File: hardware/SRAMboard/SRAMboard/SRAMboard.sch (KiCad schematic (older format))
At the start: 0 parts

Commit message: SRAMboard I
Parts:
- added C1, C2: C, Capacitor_SMD:C_0805_2012Metric, symbol Device:C
- added J1, J2: Conn_02x13_Odd_Even, Connector_PinSocket_2.54mm:PinSocket_2x13_P2.54mm_Vertical, symbol Connector_Generic:Conn_02x13_Odd_Even
- added U1: IS66WV51216EBLL-70BLI, kifootp:BGA-48_6.0x8.0mm_Layout6x8_P0.75mm, symbol kilib:IS66WV51216EBLL-70BLI
- added U2: IS66WV51216EBLL-70TLI, Package_SO:TSOP-II-44_10.16x18.41mm_P0.8mm, symbol kilib:IS66WV51216EBLL-70TLI
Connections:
- new net +3V3: C1.1, J1.20 (Pin_20), U1.D6 (VDD), U2.33 (VDD)
- new net 3V3: C2.1, J1.18 (Pin_18), U1.E1 (VDD), U2.11 (VDD)
- new net A0: J1.1 (Pin_1), U1.A3 (A0), U2.5 (A0)
- new net A1: J1.3 (Pin_3), U1.A4 (A1), U2.4 (A1)
- new net A10: J1.21 (Pin_21), U1.H4 (A10), U2.25 (A10)
- new net A11: J1.23 (Pin_23), U1.H5 (A11), U2.24 (A11)
- new net A12: J1.2 (Pin_2), U1.G3 (A12), U2.22 (A12)
- new net A13: J1.4 (Pin_4), U1.G4 (A13), U2.21 (A13)
- new net A14: J1.6 (Pin_6), U1.F3 (A14), U2.20 (A14)
- new net A15: J1.8 (Pin_8), U1.F4 (A15), U2.19 (A15)
- new net A16: J1.10 (Pin_10), U1.E4 (A16), U2.18 (A16)
- new net A17: J1.12 (Pin_12), U1.D3 (A17), U2.23 (A17)
- new net A18: J1.14 (Pin_14), U1.H1 (A18), U2.28 (A18)
- new net A2: J1.5 (Pin_5), U1.A5 (A2), U2.3 (A2)
- new net A3: J1.7 (Pin_7), U1.B3 (A3), U2.2 (A3)
- new net A4: J1.9 (Pin_9), U1.B4 (A4), U2.1 (A4)
- new net A5: J1.11 (Pin_11), U1.C3 (A5), U2.44 (A5)
- new net A6: J1.13 (Pin_13), U1.C4 (A6), U2.43 (A6)
- new net A7: J1.15 (Pin_15), U1.D4 (A7), U2.42 (A7)
- new net A8: J1.17 (Pin_17), U1.H2 (A8), U2.27 (A8)
- new net A9: J1.19 (Pin_19), U1.H3 (A9), U2.26 (A9)
- new net CS0#: J2.1 (Pin_1), U2.6 (CS1#)
- new net CS1#: J2.3 (Pin_3), U1.B5 (CS1#)
- new net CS2: J2.5 (Pin_5), U1.A6 (CS2)
- new net GND: C1.2, C2.2, J1.16 (Pin_16), J1.22 (Pin_22), U1.D1 (GND), U1.E6 (GND), U2.12 (GND), U2.34 (GND)
- new net IO0: J2.15 (Pin_15), U1.B6 (I/O0), U2.7 (I/O0)
- new net IO1: J2.17 (Pin_17), U1.C5 (I/O1), U2.8 (I/O1)
- new net IO10: J2.10 (Pin_10), U1.C2 (I/O10), U2.31 (I/O10)
- new net IO11: J2.12 (Pin_12), U1.D2 (I/O11), U2.32 (I/O11)
- new net IO12: J2.14 (Pin_14), U1.E2 (I/O12), U2.35 (I/O12)
- new net IO13: J2.16 (Pin_16), U1.F2 (I/O13), U2.36 (I/O13)
- new net IO14: J2.18 (Pin_18), U1.F1 (I/O14), U2.37 (I/O14)
- new net IO15: J2.20 (Pin_20), U1.G1 (I/O15), U2.38 (I/O15)
- new net IO2: J2.19 (Pin_19), U1.C6 (I/O2), U2.9 (I/O2)
- new net IO3: J2.21 (Pin_21), U1.D5 (I/O3), U2.10 (I/O3)
- new net IO4: J2.23 (Pin_23), U1.E5 (I/O4), U2.13 (I/O4)
- new net IO5: J2.25 (Pin_25), U1.F5 (I/O5), U2.14 (I/O5)
- new net IO6: J2.2 (Pin_2), U1.F6 (I/O6), U2.15 (I/O6)
- new net IO7: J2.4 (Pin_4), U1.G6 (I/O7), U2.16 (I/O7)
- new net IO8: J2.6 (Pin_6), U1.B1 (I/O8), U2.29 (I/O8)
- new net IO9: J2.8 (Pin_8), U1.C1 (I/O9), U2.30 (I/O9)
- new net LB#: J2.13 (Pin_13), U1.A1 (LB#), U2.39 (LB#)
- new net NC0: J2.22 (Pin_22), U1.G2 (NC)
- new net NC1: J2.24 (Pin_24), U1.E3 (NC)
- new net NC2: J2.26 (Pin_26), U1.H6 (NC)
- new net OE#: J2.7 (Pin_7), U1.A2 (OE#), U2.41 (OE#)
- new net UB#: J2.11 (Pin_11), U1.B2 (UB#), U2.40 (UB#)
- new net WE#: J2.9 (Pin_9), U1.G5 (WE#), U2.17 (WE#)
- no-connect marks 0 -> 3

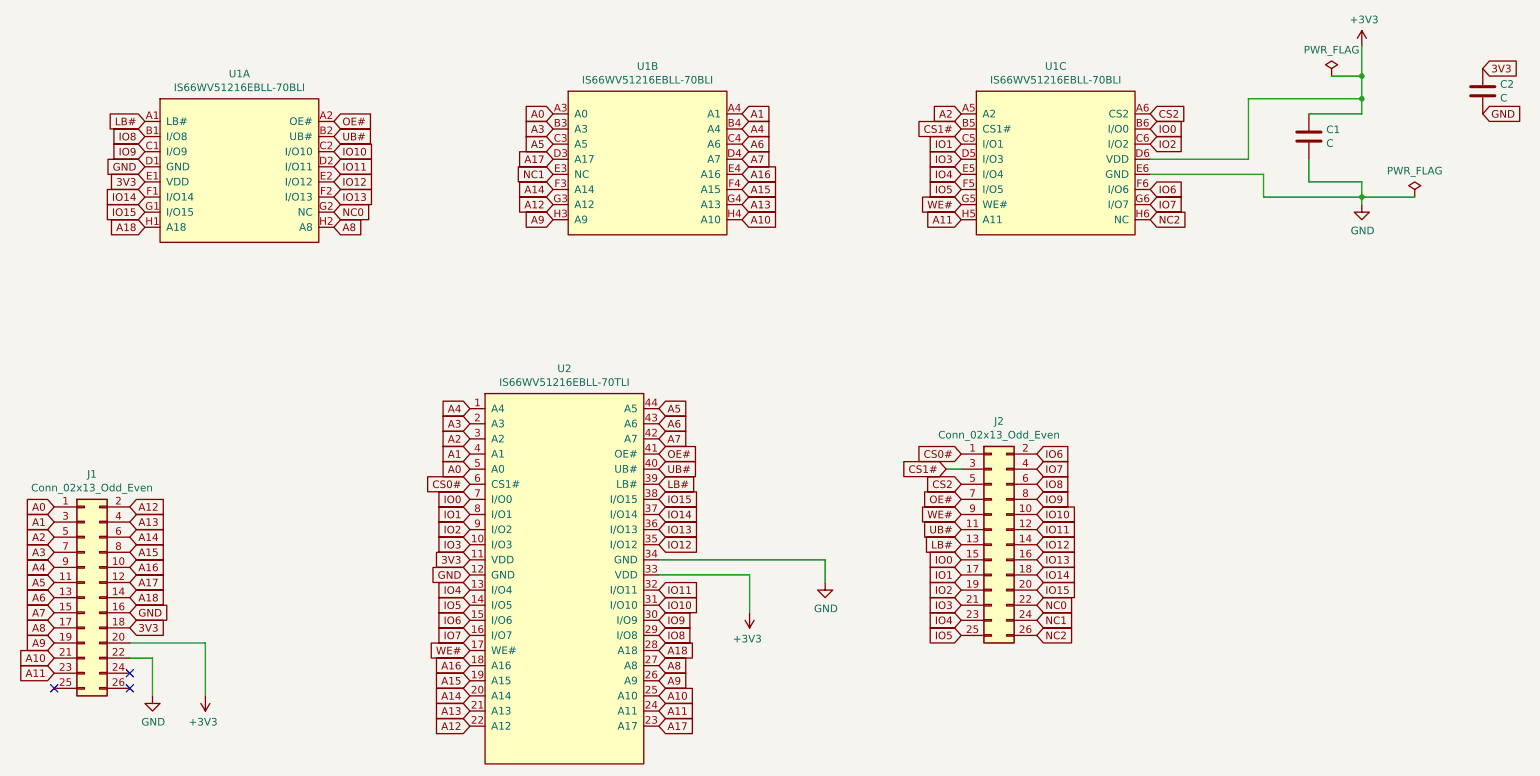
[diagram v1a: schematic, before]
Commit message: FIXED solder mask issue
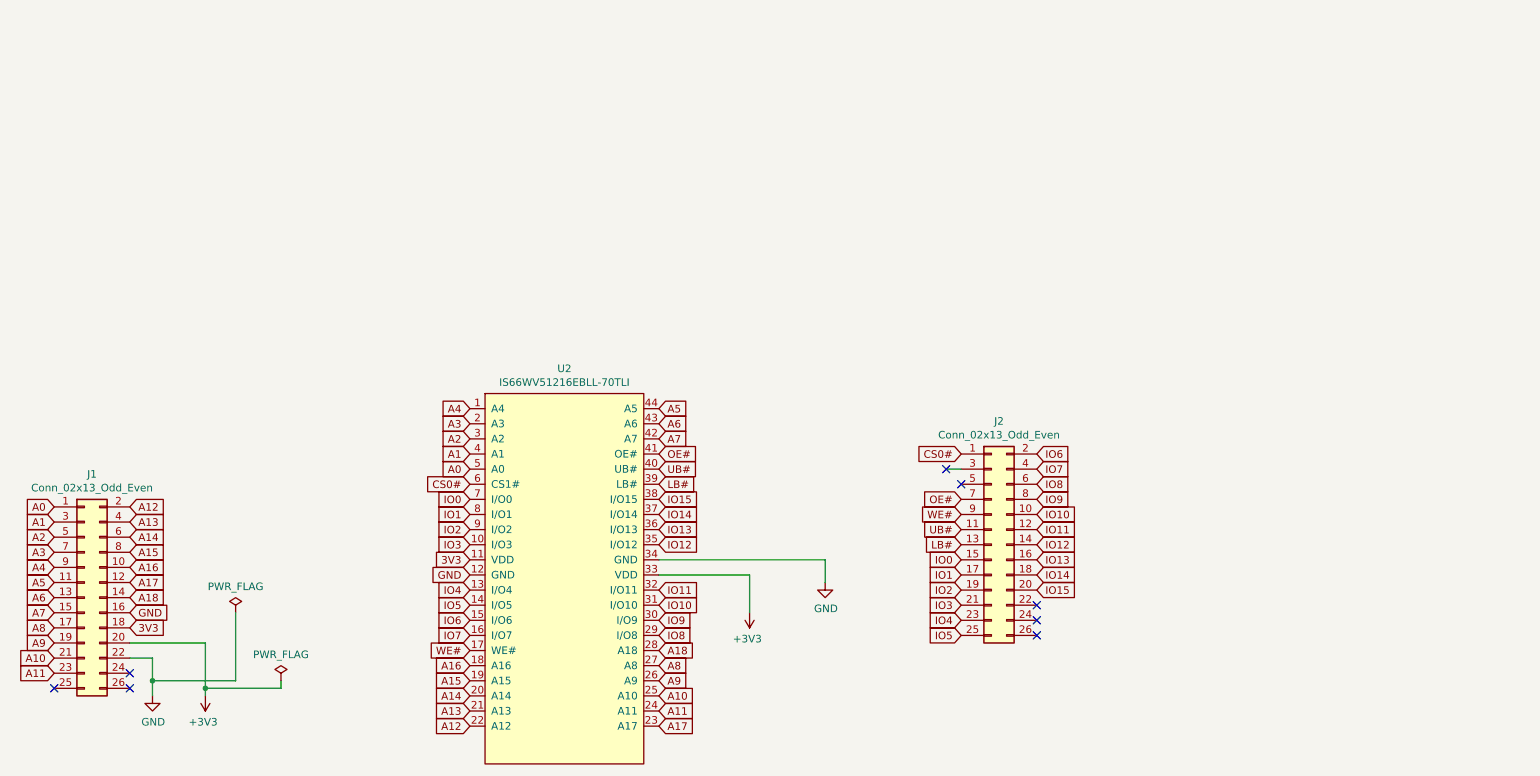
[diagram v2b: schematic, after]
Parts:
- removed C1, C2: C, Capacitor_SMD:C_0805_2012Metric, symbol Device:C
- removed U1: IS66WV51216EBLL-70BLI, kifootp:BGA-48_6.0x8.0mm_Layout6x8_P0.75mm, symbol kilib:IS66WV51216EBLL-70BLI
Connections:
- net CS1#: no longer names the net of J2.3 (Pin_3)
- net CS2: no longer names the net of J2.5 (Pin_5)
- net NC0: no longer names the net of J2.22 (Pin_22)
- net NC1: no longer names the net of J2.24 (Pin_24)
- net NC2: no longer names the net of J2.26 (Pin_26)
- no-connect marks 3 -> 8
